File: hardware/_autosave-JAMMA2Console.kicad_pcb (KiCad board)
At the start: 2 copper layers, 138 x 105 mm, 175 parts, among them J1 Conn_02x28_JAMMA, J10 Conn_02x03_Counter_Clockwise, J11 Conn_02x05_Odd_Even, J2 DB15_Female_HighDensity, J3 SCART-F, J4 DF1BZ-34DP-2.5DSA, J5 Conn_Coaxial_x2, J6 DB15_Female, J7 DB15_Female, J8 Phoenix PTS 1,5/4-5.0, J9 USB_B, U1 USBLC6-2P6, U10 74LVC4245, U11 74LVC4245, U12 TL074, U13 LM1972, U14 TPA3138D2, U15 74HCT4053, U2 LD1117-3.3, U3 74HCT4053, U4 74HCT86, U5 74HCT4053, U6 LM1881, U7 THS7375, U8 STM32F103V8Tx, U9 74LVC4245, Y1 8MHz

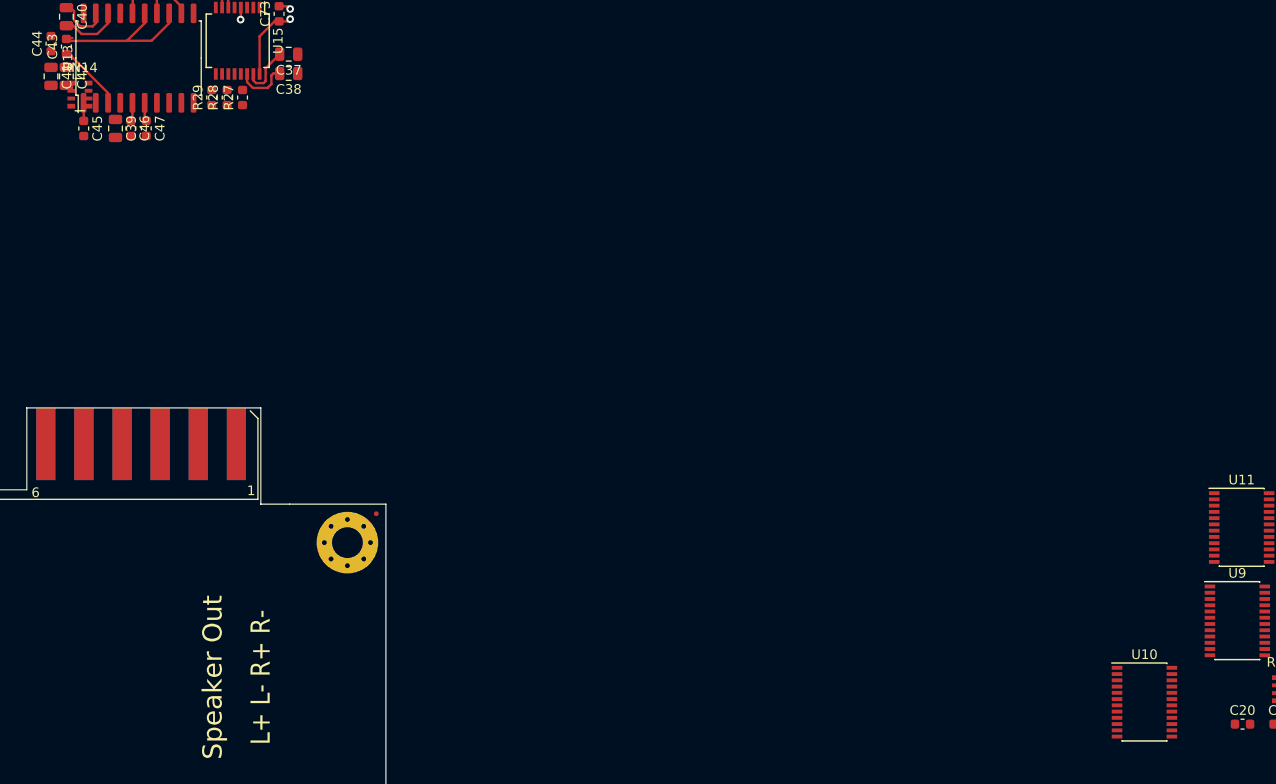
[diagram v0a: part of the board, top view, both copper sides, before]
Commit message: Schematic mainly done. Working on PCB layout in isolated blocks.
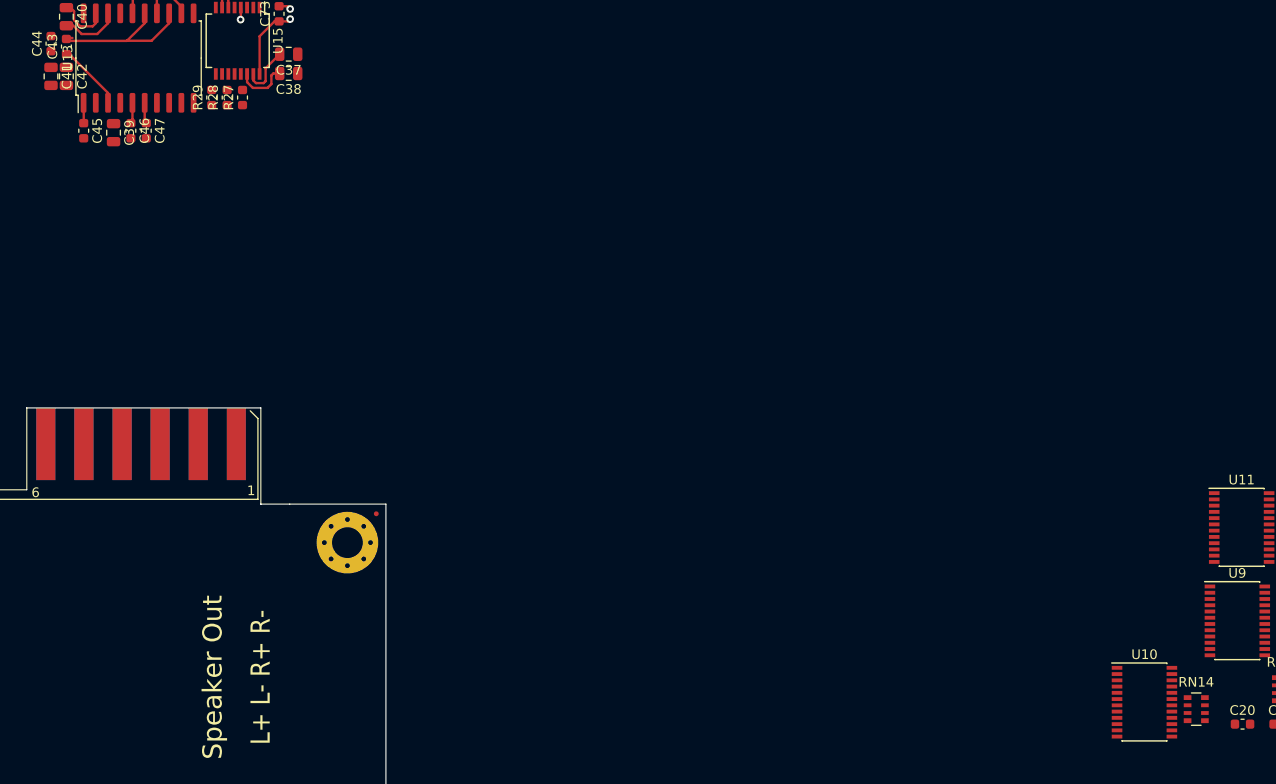
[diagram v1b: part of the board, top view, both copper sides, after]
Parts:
- moved RN14 132.4 mm to (302.2, 75.5)
- moved C39 0.48 mm to (189.7, 15.7)
- moved C46 0.25 mm to (191.5, 15.4)
- moved C47 0.25 mm to (193.1, 15.4)
- moved C45 0.24 mm to (186.6, 15.4)
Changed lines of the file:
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@@
   )
   (setup
-    (last_trace_width 2)
+    (last_trace_width 0.254)
     (user_trace_width 0.1524)
     (user_trace_width 0.2032)
@@
   )
   (module Resistor_SMD:R_Array_Convex_4x0603 (layer F.Cu)
-    (at 186.2 11.7)
+    (at 302.2 75.55)
     (descr "Chip Resistor Network, ROHM MNR14 (see mnr_g.pdf)")
     (tags "resistor array")
@@
   )
   (module Capacitor_SMD:C_0603_1608Metric (layer F.Cu)
-    (at 193.1 15.2 270)
+    (at 193.1 15.45 270)
     (descr "Capacitor SMD 0603 (1608 Metric), square (rectangular) end terminal, IPC_7351 nominal, (Body size source: http://www.tortai-tech.com/upload/download/2011102023233369053.pdf), generated with kicad-footprint-generator")
     (tags capacitor)
@@
   )
   (module Capacitor_SMD:C_0603_1608Metric (layer F.Cu)
-    (at 191.5 15.2 270)
+    (at 191.5 15.45 270)
     (descr "Capacitor SMD 0603 (1608 Metric), square (rectangular) end terminal, IPC_7351 nominal, (Body size source: http://www.tortai-tech.com/upload/download/2011102023233369053.pdf), generated with kicad-footprint-generator")
     (tags capacitor)
@@
   )
   (module Capacitor_SMD:C_0603_1608Metric (layer F.Cu)
-    (at 186.6 15.2125 270)
+    (at 186.6 15.45 270)
     (descr "Capacitor SMD 0603 (1608 Metric), square (rectangular) end terminal, IPC_7351 nominal, (Body size source: http://www.tortai-tech.com/upload/download/2011102023233369053.pdf), generated with kicad-footprint-generator")
     (tags capacitor)
@@
   )
   (module Capacitor_SMD:C_0805_2012Metric (layer F.Cu)
-    (at 189.9 15.2125 270)
+    (at 189.7 15.65 270)
     (descr "Capacitor SMD 0805 (2012 Metric), square (rectangular) end terminal, IPC_7351 nominal, (Body size source: https://docs.google.com/spreadsheets/d/1BsfQQcO9C6DZCsRaXUlFlo91Tg2WpOkGARC1WS5S8t0/edit?usp=sharing), generated with kicad-footprint-generator")
     (tags capacitor)
